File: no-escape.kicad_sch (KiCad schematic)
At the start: 115 parts, among them J1 SM04B, J2 SWD, SW1 Boot, U1 RP2040, U2 XC6206PxxxMR, U3 W25Q128JVS, U4 PRTR5V0U2X, Y1 12MHz

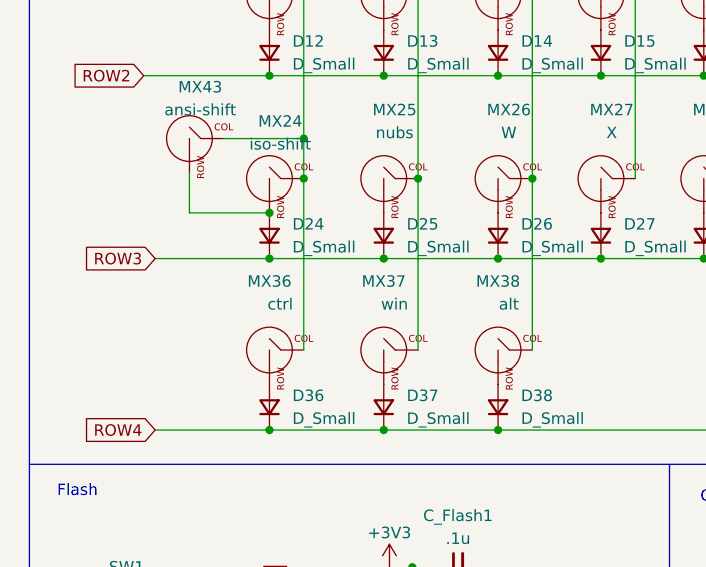
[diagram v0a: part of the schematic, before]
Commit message: add 1.5 1 bottom compatibility
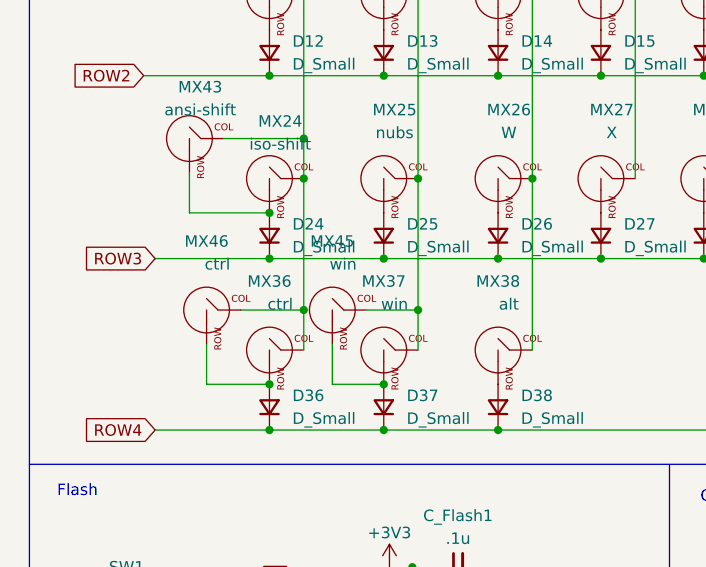
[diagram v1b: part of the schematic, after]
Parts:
- added MX45: win, parts:mx_1u, symbol lckprt:key_switch
- added MX46: ctrl, parts:mx_15u, symbol lckprt:key_switch
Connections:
- net COL1: now also MX46.1 (Passive)
- net COL2: now also MX45.1 (Passive)
- net at D37.2 (A), MX37.2 (ROW): now also MX45.2 (ROW)
- net at D36.2 (A), MX36.2 (ROW): now also MX46.2 (ROW)
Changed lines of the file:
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@@
   (junction (at 68.58 53.34) (diameter 0) (color 0 0 0 0)
   )
+  (junction (at 39.37 96.52) (diameter 0) (color 0 0 0 0)
+  )
   (junction (at 80.01 33.02) (diameter 0) (color 0 0 0 0)
   )
@@
   (junction (at 87.63 41.91) (diameter 0) (color 0 0 0 0)
   )
+  (junction (at 55.88 88.265) (diameter 0) (color 0 0 0 0)
+  )
   (junction (at 121.92 62.23) (diameter 0) (color 0 0 0 0)
   )
@@
   (junction (at 114.3 88.9) (diameter 0) (color 0 0 0 0)
   )
+  (junction (at 43.18 88.265) (diameter 0) (color 0 0 0 0)
+  )
   (junction (at 181.61 115.57) (diameter 0) (color 0 0 0 0)
   )
@@
   (junction (at 110.49 82.55) (diameter 0) (color 0 0 0 0)
   )
+  (junction (at 52.07 96.52) (diameter 0) (color 0 0 0 0)
+  )
   (junction (at 76.2 82.55) (diameter 0) (color 0 0 0 0)
   )
@@
     (stroke (width 0) (type default))
   )
+  (wire (pts (xy 36.195 88.265) (xy 43.18 88.265))
+    (stroke (width 0) (type default))
+  )
   (wire (pts (xy 114.3 143.51) (xy 116.84 143.51))
     (stroke (width 0) (type default))
@@
     (stroke (width 0) (type default))
   )
+  (wire (pts (xy 46.355 96.52) (xy 52.07 96.52))
+    (stroke (width 0) (type default))
+  )
   (wire (pts (xy 185.42 44.45) (xy 180.34 44.45))
     (stroke (width 0) (type default))
@@
     (stroke (width 0) (type default))
   )
+  (wire (pts (xy 55.88 88.265) (xy 55.88 92.71))
+    (stroke (width 0) (type default))
+  )
   (wire (pts (xy 148.59 33.02) (xy 148.59 53.34))
     (stroke (width 0) (type default))
@@
     (stroke (width 0) (type default))
   )
+  (wire (pts (xy 50.165 88.265) (xy 55.88 88.265))
+    (stroke (width 0) (type default))
+  )
   (polyline (pts (xy 186.69 12.7) (xy 12.7 12.7))
     (stroke (width 0) (type default))
@@
     (stroke (width 0) (type default))
   )
+  (wire (pts (xy 46.355 92.075) (xy 46.355 96.52))
+    (stroke (width 0) (type default))
+  )
   (wire (pts (xy 104.14 120.65) (xy 104.14 125.73))
     (stroke (width 0) (type default))
@@
     (stroke (width 0) (type default))
   )
-  (wire (pts (xy 55.88 73.66) (xy 55.88 92.71))
+  (wire (pts (xy 55.88 73.66) (xy 55.88 88.265))
+    (stroke (width 0) (type default))
+  )
+  (wire (pts (xy 32.385 92.075) (xy 32.385 96.52))
     (stroke (width 0) (type default))
   )
@@
     (stroke (width 0) (type default))
   )
+  (wire (pts (xy 43.18 88.265) (xy 43.18 92.71))
+    (stroke (width 0) (type default))
+  )
   (wire (pts (xy 105.41 173.99) (xy 105.41 184.15))
     (stroke (width 0) (type default))
@@
     (stroke (width 0) (type default))
   )
+  (wire (pts (xy 32.385 96.52) (xy 39.37 96.52))
+    (stroke (width 0) (type default))
+  )
   (wire (pts (xy 218.44 107.95) (xy 220.98 107.95))
     (stroke (width 0) (type default))
@@
     (stroke (width 0) (type default))
   )
-  (wire (pts (xy 43.18 73.66) (xy 43.18 92.71))
+  (wire (pts (xy 43.18 73.66) (xy 43.18 88.265))
     (stroke (width 0) (type default))
   )
@@
     )
   )
+  (symbol (lib_id "lckprt:key_switch") (at 46.355 88.265 0) (unit 1)
+    (in_bom yes) (on_board yes) (dnp no)
+    (property "Reference" "MX45" (at 46.355 80.645 0)
+      (effects (font (size 1.27 1.27)))
+    )
+    (property "Value" "win" (at 47.5581 83.185 0)
+      (effects (font (size 1.27 1.27)))
+    )
+    (property "Footprint" "parts:mx_1u" (at 46.355 88.265 0)
+      (effects (font (size 1.27 1.27)) hide)
+    )
+    (property "Datasheet" "" (at 46.355 88.265 0)
+      (effects (font (size 1.27 1.27)) hide)
+    )
+    (pin "1")
+    (pin "2")
+    (instances
+      (project "no-escape"
+        (path "/277e8569-6c28-4d54-96df-2e9800302384"
+          (reference "MX45") (unit 1)
+        )
+      )
+    )
+  )
   (symbol (lib_id "lckprt:key_switch") (at 64.77 33.02 0) (unit 1)
     (in_bom yes) (on_board yes) (dnp no) (fields_autoplaced)
@@
         )
       )
+    )
+  )
+  (symbol (lib_id "lckprt:key_switch") (at 32.385 88.265 0) (unit 1)
+    (in_bom yes) (on_board yes) (dnp no)
+    (property "Reference" "MX46" (at 32.385 80.645 0)
+      (effects (font (size 1.27 1.27)))
+    )
+    (property "Value" "ctrl" (at 33.5881 83.185 0)
+      (effects (font (size 1.27 1.27)))
+    )
+    (property "Footprint" "parts:mx_15u" (at 32.385 88.265 0)
+      (effects (font (size 1.27 1.27)) hide)
+    )
+    (property "Datasheet" "" (at 32.385 88.265 0)
+      (effects (font (size 1.27 1.27)) hide)
+    )
+    (pin "1")
+    (pin "2")
+    (instances
+      (project "no-escape"
+        (path "/277e8569-6c28-4d54-96df-2e9800302384"
+          (reference "MX46") (unit 1)
+        )
+      )

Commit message: add Druz's review
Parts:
- removed J2: SWD, Connector_PinHeader_2.54mm:PinHeader_1x05_P2.54mm_Vertical, symbol Connector:Conn_01x05_Female
- added D41, D42: D_Small, Diode_SMD:D_SOD-123, symbol Device:D_Small
- added J2: reset, Connector_PinHeader_2.54mm:PinHeader_1x02_P2.54mm_Vertical, symbol Connector:Conn_01x02_Socket
- added J3: JST, Connector_JST:JST_SH_SM04B-SRSS-TB_1x04-1MP_P1.00mm_Horizontal, symbol Connector:Conn_01x04_Female
- added MX47: alt-1.5, parts:mx_15u, symbol lckprt:key_switch
- added MX48: space-2.75, parts:mx_275u_reverse, symbol lckprt:key_switch
- added MX49: space-2.25, parts:mx_225u, symbol lckprt:key_switch
- added MX50: space-1.5, parts:mx_15u, symbol lckprt:key_switch
- J1: value SM04B -> MOLEX
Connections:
- net +5V: now also J3.1 (Pin_1)
- net COL10: now also U1.5 (GPIO3), MX50.1 (Passive); no longer U1.6 (GPIO4)
- net COL11: now also U1.4 (GPIO2); no longer U1.7 (GPIO5)
- net COL12: now also U1.3 (GPIO1); no longer U1.8 (GPIO6)
- net COL3: now also MX47.1 (Passive)
- net COL6: now also U1.9 (GPIO7), MX48.1 (Passive); no longer U1.2 (GPIO0)
- net COL7: now also U1.8 (GPIO6), MX49.1 (Passive); no longer U1.3 (GPIO1)
- net COL8: now also U1.7 (GPIO5); no longer U1.4 (GPIO2)
- net COL9: now also U1.6 (GPIO4); no longer U1.5 (GPIO3)
- net D+: now also J3.3 (Pin_3)
- net D-: now also J3.2 (Pin_2)
- net GND: now also J2.2 (Pin_2), J3.4 (Pin_4)
- net RESET: now also J2.1 (Pin_1)
- net ROW1: now also U1.18 (GPIO15); no longer U1.29 (GPIO18)
- net ROW2: now also U1.17 (GPIO14); no longer U1.30 (GPIO19)
- net ROW3: now also U1.16 (GPIO13); no longer U1.31 (GPIO20)
- net ROW4: now also U1.15 (GPIO12), D41.1 (K), D42.1 (K); no longer U1.32 (GPIO21)
- net at D39.2 (A), MX39.2 (ROW), MX44.2 (ROW): now also MX49.2 (ROW)
- net at D38.2 (A), MX38.2 (ROW): now also MX47.2 (ROW)
- new net: D42.2 (A), MX50.2 (ROW)
- new net: D41.2 (A), MX48.2 (ROW)
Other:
- added sheet c3_db (c3_db.kicad_sch)
- moved on the sheet: MX44

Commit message: Silkscreen alignment, fixes
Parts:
- added MX51: space, parts:mx_7u, symbol lckprt:key_switch
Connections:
- net COL7: now also MX51.1 (Passive)
- net at D39.2 (A), MX39.2 (ROW), MX44.2 (ROW)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: now also MX51.2 (ROW)
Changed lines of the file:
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@@
   (junction (at 52.07 62.23) (diameter 0) (color 0 0 0 0)
   )
+  (junction (at 125.73 85.09) (diameter 0) (color 0 0 0 0)
+  )
   (junction (at 160.02 73.66) (diameter 0) (color 0 0 0 0)
   )
@@
   (junction (at 91.44 179.07) (diameter 0) (color 0 0 0 0)
   )
+  (junction (at 121.92 96.52) (diameter 0) (color 0 0 0 0)
+  )
   (junction (at 171.45 44.45) (diameter 0) (color 0 0 0 0)
   )
@@
     (stroke (width 0) (type default))
   )
+  (wire (pts (xy 135.255 92.71) (xy 135.255 85.09))
+    (stroke (width 0) (type default))
+  )
   (polyline (pts (xy 83.82 156.21) (xy 151.13 156.21))
     (stroke (width 0) (type default))
@@
     (stroke (width 0) (type default))
   )
+  (wire (pts (xy 135.255 85.09) (xy 125.73 85.09))
+    (stroke (width 0) (type default))
+  )
   (wire (pts (xy 156.21 62.23) (xy 167.64 62.23))
     (stroke (width 0) (type default))
@@
     (stroke (width 0) (type default))
   )
+  (wire (pts (xy 121.92 96.52) (xy 131.445 96.52))
+    (stroke (width 0) (type default))
+  )
   (wire (pts (xy 114.3 88.9) (xy 114.3 92.71))
     (stroke (width 0) (type default))
@@
         )
       )
+    )
+  )
+  (symbol (lib_id "lckprt:key_switch") (at 131.445 92.71 0) (unit 1)
+    (in_bom yes) (on_board yes) (dnp no)
+    (property "Reference" "MX51" (at 131.445 85.09 0)
+      (effects (font (size 1.27 1.27)))
+    )
+    (property "Value" "space" (at 132.6481 87.63 0)
+      (effects (font (size 1.27 1.27)))
+    )
+    (property "Footprint" "parts:mx_7u" (at 131.445 92.71 0)
+      (effects (font (size 1.27 1.27)) hide)
+    )
+    (property "Datasheet" "" (at 131.445 92.71 0)
+      (effects (font (size 1.27 1.27)) hide)
+    )
+    (pin "1")
+    (pin "2")
+    (instances
+      (project "no-escape"
+        (path "/277e8569-6c28-4d54-96df-2e9800302384"
+          (reference "MX51") (unit 1)
+        )
+      )
